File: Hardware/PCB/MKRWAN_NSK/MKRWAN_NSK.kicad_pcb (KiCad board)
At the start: 2 copper layers, 70.5 x 84 mm, 19 parts, among them J10 O2_Sensor, J11 Extra_1, J12 TTL, J13 Pont_diviseur, J14 Conn_01x06, J15 Conn_01x06, J2 TH_Deep_Sensor, J3 Other_Gaz_Sensor, J4 UV_IR_Sensor, J5 Extra_2, J6 RGB_Sensor, J7 CO2_Sensor, J8 Pressure_Sensor, J9 TH_Surface_Sensor, U1 ARDUINO_MKR_WAN_1310

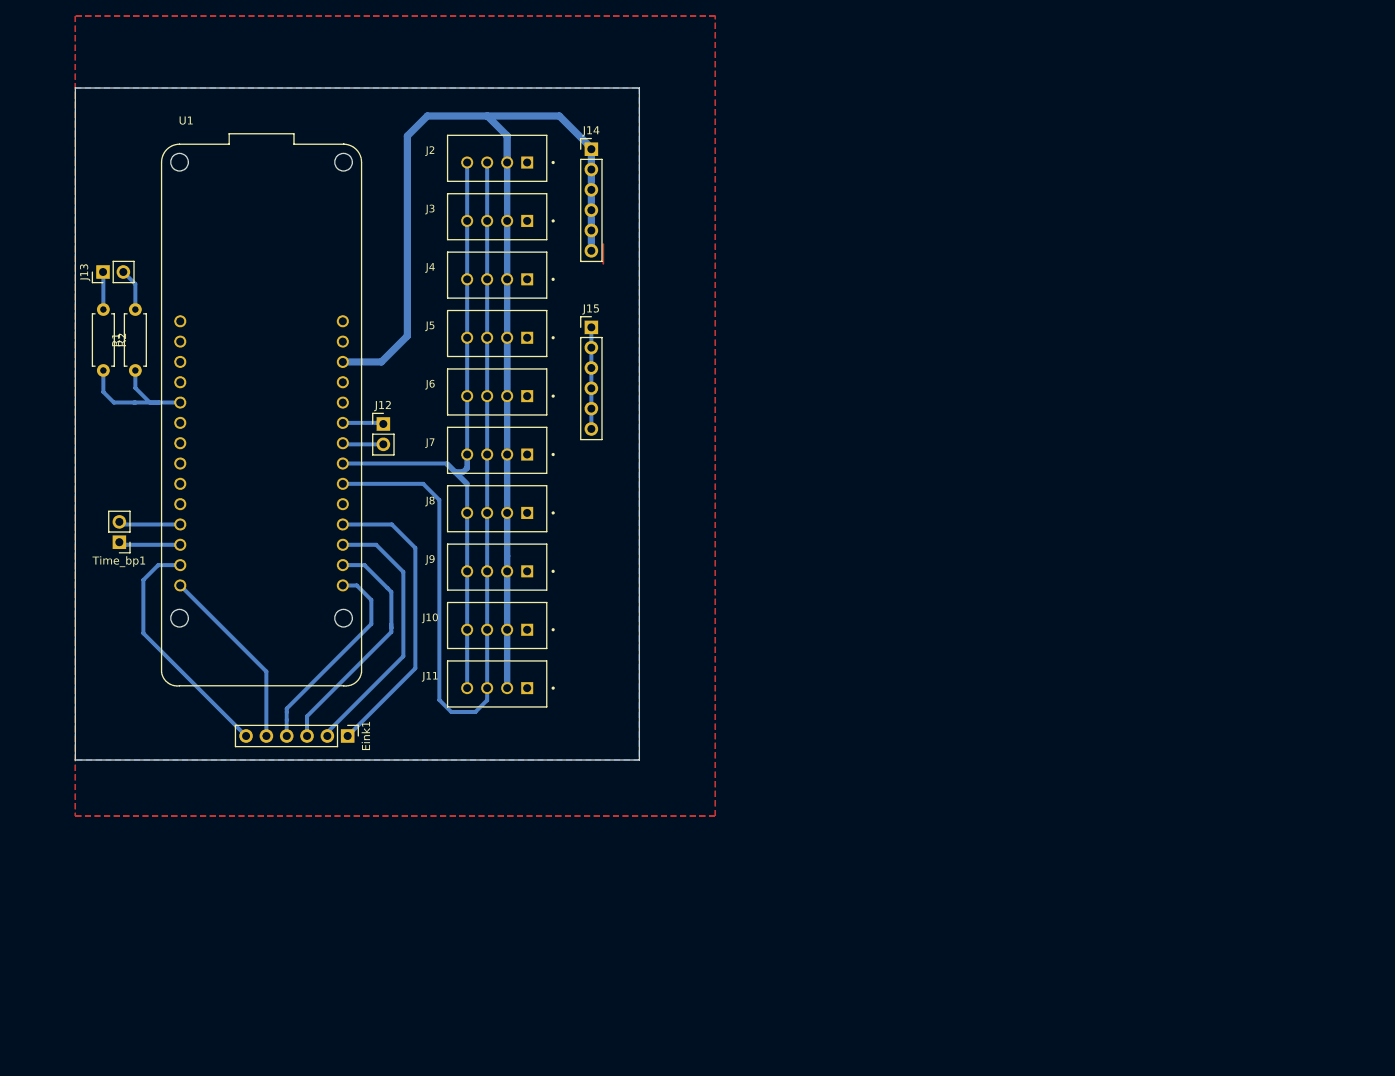
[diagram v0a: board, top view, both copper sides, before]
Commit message: Hardware PCB - PCB v4 TTL + Timer + Boster + Level Shifter
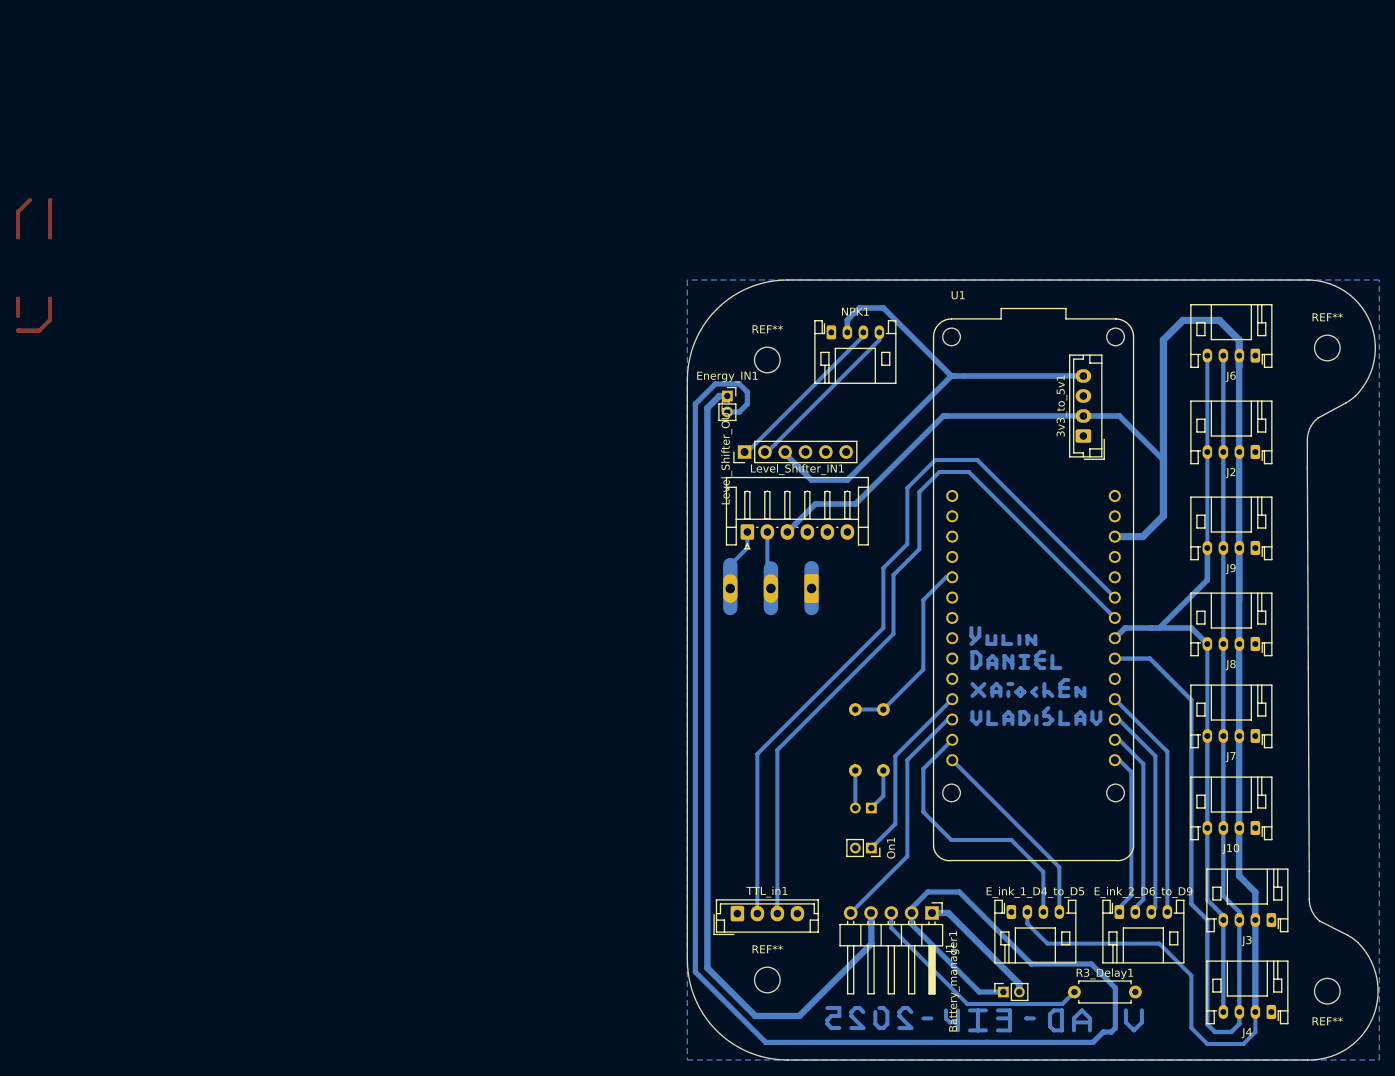
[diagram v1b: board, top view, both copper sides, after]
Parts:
- removed Eink1, J14, J15: Conn_01x06, Connector_PinHeader_2.54mm:PinHeader_1x06_P2.54mm_Vertical
- removed J11: Extra_1, B4B-XH-A_LF__SN_:JST_B4B-XH-A_LF__SN_
- removed J12: TTL, Connector_PinHeader_2.54mm:PinHeader_1x02_P2.54mm_Vertical
- removed J5: Extra_2, B4B-XH-A_LF__SN_:JST_B4B-XH-A_LF__SN_
- added 3v3_to_5v1: Conn_01x04, Connector_JST:JST_EH_B4B-EH-A_1x04_P2.50mm_Vertical, F.Cu at (226.0, 82.5)
- added Battery_manager1: ~, Connector_PinSocket_2.00mm:PinSocket_1x02_P2.00mm_Vertical, F.Cu at (216.0, 152.0)
- added E_ink_1_D4_to_D5: S4B-PH-K-S_LF__SN_, Connector_JST:JST_PH_S4B-PH-K_1x04_P2.00mm_Horizontal, F.Cu at (217.0, 142.0)
- added E_ink_2_D6_to_D9: S4B-PH-K-S_LF__SN_, Connector_JST:JST_PH_S4B-PH-K_1x04_P2.00mm_Horizontal, F.Cu at (230.5, 142.0)
- added Energy_IN1: Pont_diviseur, Connector_PinSocket_2.00mm:PinSocket_1x02_P2.00mm_Vertical, F.Cu at (181.5, 77.5)
- added J1: Conn_01x05, Connector_PinHeader_2.54mm:PinHeader_1x05_P2.54mm_Horizontal, F.Cu at (207.1, 142.1)
- added Level_Shifter_IN1: Conn_01x06, Connector_JST:JST_EH_S6B-EH_1x06_P2.50mm_Horizontal, F.Cu at (184.0, 94.5)
- added Level_Shifter_OUT1: Conn_01x06, Connector_PinHeader_2.54mm:PinHeader_1x06_P2.54mm_Vertical, F.Cu at (183.7, 84.5)
- added NPK1: S4B-PH-K-S_LF__SN_, Connector_JST:JST_PH_S4B-PH-K_1x04_P2.00mm_Horizontal, F.Cu at (194.5, 69.5)
- added R3_Delay1: R_US, Resistor_THT:R_Axial_DIN0207_L6.3mm_D2.5mm_P7.62mm_Horizontal, F.Cu at (224.9, 152.0)
- added REF**: MountingHole_3.2mm_M3_DIN965, MountingHole:MountingHole_3.2mm_M3_DIN965, F.Cu at (186.5, 73.0)
- added REF**: MountingHole_3.2mm_M3_DIN965, MountingHole:MountingHole_3.2mm_M3_DIN965, F.Cu at (186.5, 150.5)
- added REF**: MountingHole_3.2mm_M3_DIN965, MountingHole:MountingHole_3.2mm_M3_DIN965, F.Cu at (256.5, 151.9)
- added REF**: MountingHole_3.2mm_M3_DIN965, MountingHole:MountingHole_3.2mm_M3_DIN965, F.Cu at (256.5, 71.5)
- added TLL_out1: Conn_01x03, Connector_Phoenix_MC_HighVoltage:PhoenixContact_MC_1,5_3-G-5.08_1x03_P5.08mm_Horizontal, B.Cu at (192.0, 101.6)
- added TTL_in1: Conn_01x04, Connector_JST:JST_EH_B4B-EH-A_1x04_P2.50mm_Vertical, F.Cu at (182.8, 142.2)
- J10, J2, J3, J4, J6, J7, J8, J9: footprint B4B-XH-A_LF__SN_:JST_B4B-XH-A_LF__SN_ -> Connector_JST:JST_PH_S4B-PH-K_1x04_P2.00mm_Horizontal
- J13: footprint Connector_PinHeader_2.54mm:PinHeader_1x02_P2.54mm_Vertical -> Connector_PinSocket_2.00mm:PinSocket_1x02_P2.00mm_Vertical; moved to B.Cu
- On1: renamed from Time_bp1; value Conn_01x02 -> Off; footprint Connector_PinHeader_2.54mm:PinHeader_1x02_P2.54mm_Vertical -> Connector_PinSocket_2.00mm:PinSocket_1x02_P2.00mm_Vertical
- R1, R2: moved to B.Cu
- moved J4 133.6 mm to (249.5, 154.5), turned to 180 degrees
- moved J3 130.7 mm to (249.5, 143.0), turned to 180 degrees
- moved J13 117.1 mm to (199.5, 129.0)
- moved R2 113.3 mm to (201.0, 124.3), turned to 90 degrees
- moved J2 101.6 mm to (247.5, 84.5), turned to 180 degrees
- moved On1 101.5 mm to (199.5, 134.0), turned to -90 degrees
- moved J7 101.3 mm to (247.5, 120.0), turned to 180 degrees
- moved R1 99.5 mm to (197.5, 116.7), turned to -90 degrees
- moved U1 98.9 mm to (219.8, 101.7)
- moved J10 98.1 mm to (247.5, 131.5), turned to 180 degrees
- moved J8 96.3 mm to (247.5, 108.5), turned to 180 degrees
- moved J6 94.9 mm to (247.5, 72.5), turned to 180 degrees
- moved J9 94.8 mm to (247.5, 96.5), turned to 180 degrees
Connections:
- On1 pad 1: /D3 -> /D2
- On1 pad 2: /D2 -> /GND
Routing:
- net /GND_bis: track 0.00 -> 193.8 mm
- net /3v3_bis: track 0.00 -> 103.7 mm
- net /TX_D14: track 5.12 -> 95.5 mm
- net /GND: track 18.0 -> 107.3 mm
- net /RX_D13: track 5.12 -> 93.1 mm
- net /3v3: track 161.5 -> 239.0 mm
- net /5v: track 0.00 -> 63.4 mm
- net Net-(Battery_manager1-Pin_2): track 0.00 -> 57.4 mm
- net /SDA: track 112.3 -> 142.3 mm
- net Net-(J1-Pin_3): track 0.00 -> 29.3 mm
- net (no net): track 0.00 -> 24.6 mm
- net /D3: track 7.75 -> 29.8 mm
- net /A_5v: track 0.00 -> 21.3 mm
- net /B_5v: track 0.00 -> 21.1 mm
- net /D2: track 7.75 -> 22.8 mm
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- removed copper zone on F.Cu, net /GND
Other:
- board size 70.5 x 84 mm -> 86.3 x 97.5 mm
- board text added: "TH_Surface_Sensor"
